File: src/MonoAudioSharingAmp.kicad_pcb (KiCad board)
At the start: 2 copper layers, 90.2 x 38.1 mm, 49 parts, among them J1 CONN_5, J2 CONN_5, K1 CONN_5, K2 CONN_5, K3 CONN_5, K4 CONN_5, P1 CONN_2X2, P2 CONN_2X2, U1 LP5907, U2 DUAL_OPAMP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

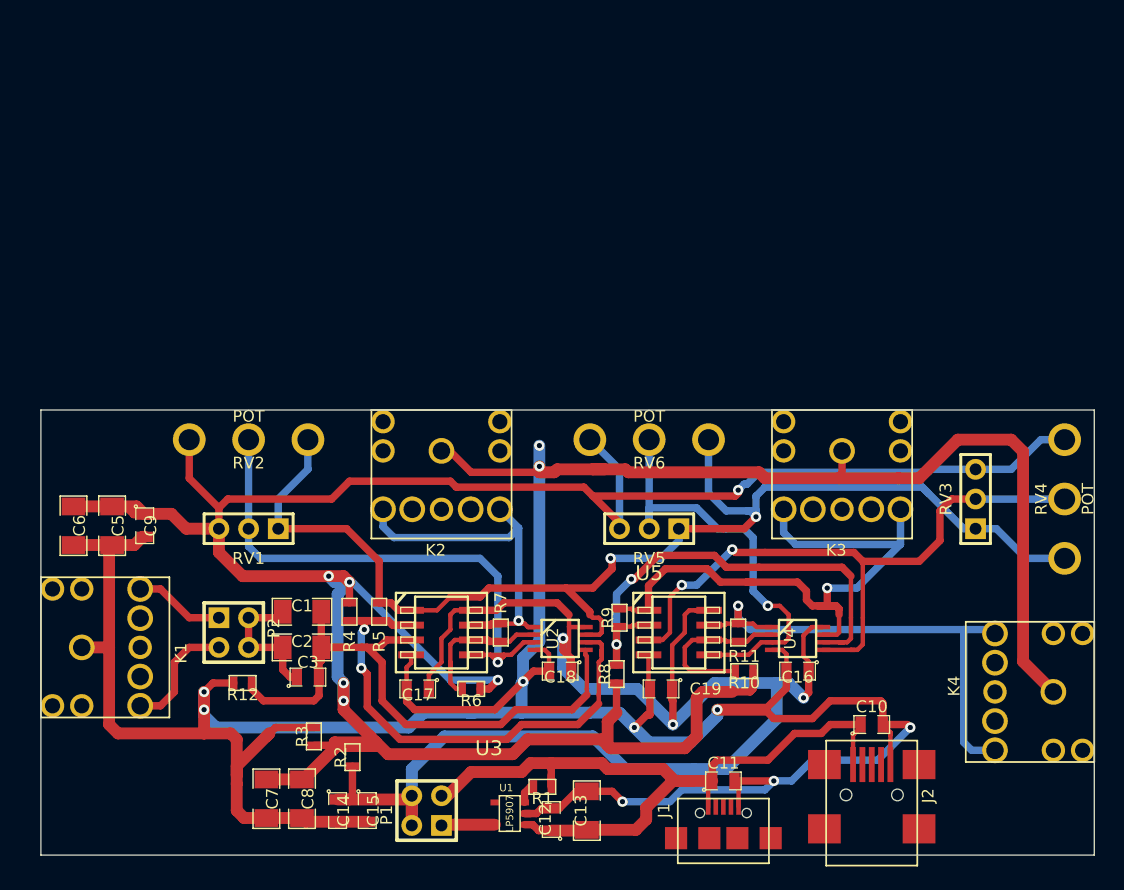
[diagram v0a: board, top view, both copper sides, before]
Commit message: Added mounting hole. Added text messages. Enlarged the board.
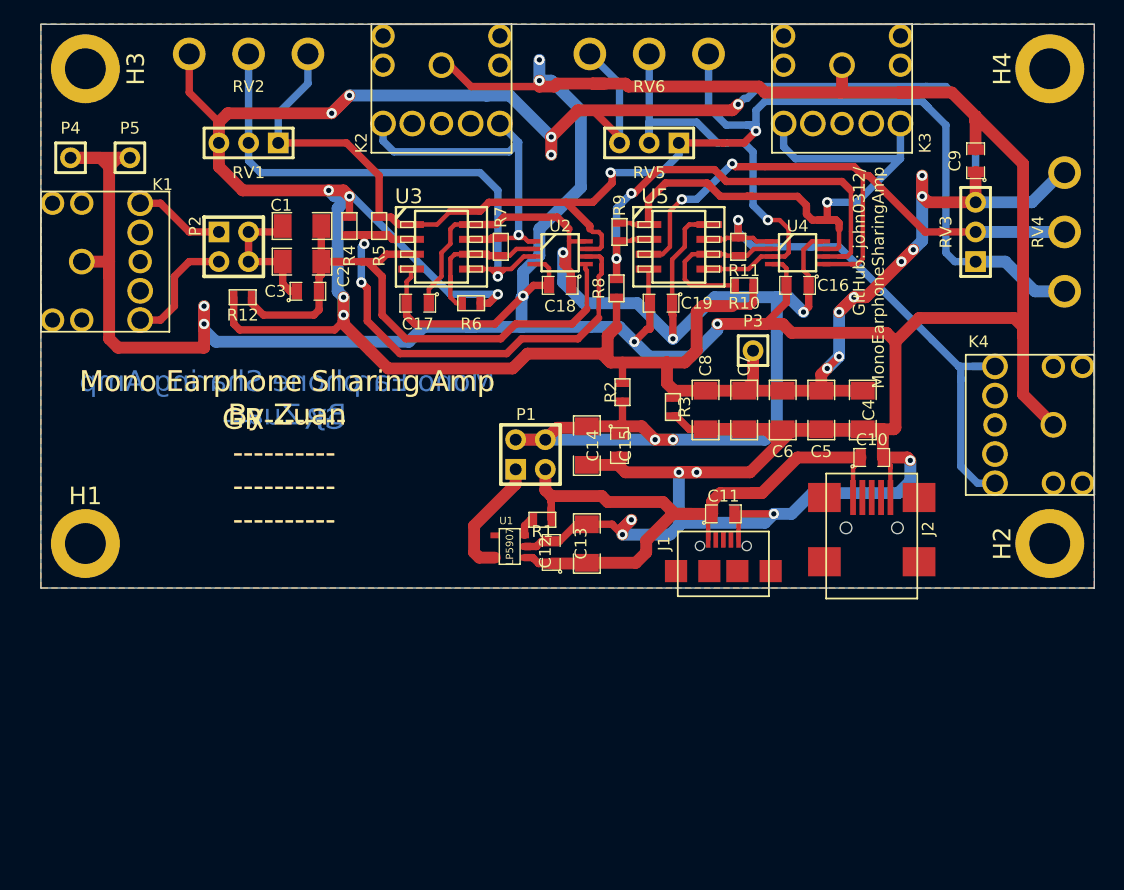
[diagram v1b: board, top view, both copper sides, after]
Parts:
- added C4: CAPAPOL, SM1206-XLTXT, F.Cu at (146.6, 109.2)
- added H1: CONN_1, M3_SCREW, F.Cu at (80.0, 120.7)
- added H2: CONN_1, M3_SCREW, F.Cu at (162.6, 120.7)
- added H3: CONN_1, M3_SCREW, F.Cu at (80.0, 80.0)
- added H4: CONN_1, M3_SCREW, F.Cu at (162.6, 80.0)
- added P3: CONN_1, PIN_ARRAY_1x1_XLPAD, F.Cu at (137.2, 104.1)
- added P4: CONN_1, PIN_ARRAY_1x1_XLPAD, F.Cu at (78.7, 87.6)
- added P5: CONN_1, PIN_ARRAY_1x1_XLPAD, F.Cu at (83.8, 87.6)
- C14: footprint SM0805-XLTXT -> SM1206-XLTXT
- moved C9 77.7 mm to (156.2, 87.9), turned to 90 degrees
- moved C5 61.5 mm to (143.0, 109.2)
- moved C6 61.5 mm to (139.7, 109.2)
- moved C7 52.7 mm to (136.4, 109.2)
- moved C8 48.0 mm to (133.1, 109.2)
- moved R3 41.7 mm to (130.3, 109.0), turned to 270 degrees
- moved R2 38.9 mm to (126.0, 107.7)
- moved C15 38.0 mm to (125.7, 112.3)
- moved C14 37.8 mm to (122.9, 112.3)
- moved C1 33.0 mm to (98.6, 93.5)
- moved C17 33.0 mm to (108.5, 100.1)
- moved C19 33.0 mm to (129.3, 100.1)
- moved C3 33.0 mm to (99.1, 99.1)
- moved P2 33.0 mm to (92.7, 95.2)
- moved R11 33.0 mm to (135.9, 95.2)
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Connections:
- R12 pad 2: GND -> /VGND
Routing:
- net GND: track 327.7 -> 433.9 mm, vias 10 -> 13
- net /VGND: track 306.9 -> 404.8 mm, vias 6 -> 18
- net /PreA_Out: track 108.5 -> 119.1 mm
- net /Power/USB_5V: track 86.3 -> 79.6 mm
- net /ChC_Out: track 43.3 -> 49.6 mm
- net /Power/Vcc: track 161.3 -> 155.0 mm, vias 3 -> 5
- net /Power/Filtered_Vcc: track 4.87 -> 10.5 mm
- net /ChB_NI: track 56.3 -> 54.8 mm
- added copper zone on B.Cu, net GND
- added copper zone on F.Cu, net GND
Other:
- board size 90.2 x 38.1 mm -> 90.2 x 48.3 mm
- net class Default: trace_width 0.635 -> 1.016
- board text added: "GR-------- ---------- ---------- ----------"
- board text added: "GitHub: john0312/ MonoEarphoneSharingAmp"
- board text added: "Mono Earphone Sharing Amp By Zuan"
